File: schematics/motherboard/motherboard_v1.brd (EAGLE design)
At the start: 50 x 50 mm, 66 parts, among them IC1 3.3V, SW1 A6H2101, Y1 25MHz

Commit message: MB PCB update
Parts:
- removed JP5: JTAG_CONNPTH, connectors:AVR_ICSP
- removed JP8: (no value), SparkFun-Retired:SJ_2S-NO
- removed U$2: (no value), Skippy-ExtBoards:BTM400_6B
- added JP26, JP27: (no value), SparkFun-Connectors:1X05
- C15, C3, C4, C5, C6, C9: device SparkFun-Capacitors:1206 -> SparkFun-Capacitors:0805
- JP11: value NEO-6M -> (none); device Skippy-ExtBoards:G6-GPS6MV2 -> SparkFun-Connectors:1X05
- moved JP18 137.7 mm to (44.2, 18.5), turned to 180 degrees
- moved JP17 124.6 mm to (44.2, 28.4), turned to 180 degrees
- moved JP4 120.5 mm to (34.0, 6.35)
- moved JP1 120.3 mm to (46.5, 6.35)
- moved JP3 120.3 mm to (40.1, 6.35)
- moved JP16 117.8 mm to (44.2, 21.8), turned to 180 degrees
- moved C13 116.9 mm to (16.5, 18.5), flipped to the bottom, turned to 135 degrees
- moved D2 116.1 mm to (45.2, 41.4), turned to 90 degrees
- moved C12 115.7 mm to (18.5, 16.5), flipped to the bottom, turned to 135 degrees
- moved C15 115.5 mm to (15.5, 27.4), flipped to the bottom, turned to 45 degrees
- moved JP24 113.2 mm to (48.3, 43.4), turned to 270 degrees
- moved R13 112.5 mm to (5.08, 18.0), flipped to the bottom, turned to 90 degrees
- moved R12 112.5 mm to (5.08, 12.4), flipped to the bottom, turned to 270 degrees
- moved JP15 107.2 mm to (44.2, 25.1), turned to 180 degrees
- moved C10 106.0 mm to (22.1, 23.9), flipped to the bottom, turned to 315 degrees
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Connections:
- removed net JTDO3_TDI2: JP5.9
- removed net JTDO3_TDI4: JP4.3, JP8.1
- new net US_ECHO: JP11.3, U$1.36
- new net US_TRIGGER: JP11.4, U$1.35
- net 3.3V: now also JP26.4, JP27.4; no longer JP11.4, JP5.4, U$2.3.3V
- net DBG_CMD: now also JP26.1; no longer U$2.PIO(11)
- net GND: now also JP26.5, JP27.5; no longer JP5.10, JP5.2, U$2.GND@1, U$2.GND@2, U$2.GND@3, U$2.GND@4
- net JTCK: no longer JP5.1
- net JTDOM: now also JP4.3; no longer JP5.3, JP8.2
- net JTMS: no longer JP5.5
- net RX1: now also JP27.2; no longer JP11.2
- net RX2: now also JP26.2; no longer U$2.UART-TX
- net TX1: now also JP27.3; no longer JP11.3
- net TX2: now also JP26.3; no longer U$2.UART-RX
- net VDD: now also JP11.5
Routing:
- net 3.3V: track 0.00 -> 39.8 mm, vias 0 -> 1
- net GND: track 0.00 -> 21.2 mm, vias 0 -> 3
- net N$3: track 0.00 -> 17.2 mm, vias 0 -> 1
- net N$5: track 0.00 -> 16.4 mm, vias 0 -> 1
- added copper zone on layer 16, net GND

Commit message: Motherboard update with almost-ready routing
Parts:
- added H1, H2, H3, H4: MOUNT-PAD-ROUND3.0, holes:3,0-PAD
- added U$2: SKIPPYTXT-PLC-10MM, skippy-logo:SKIPPYTXT-PLC-10MM
- moved R11 107.4 mm to (45.2, 38.7), turned to 270 degrees
- moved R10 102.6 mm to (45.2, 38.7), flipped to the bottom, turned to 270 degrees
- moved JP25 97.8 mm to (45.3, 33.9), flipped to the bottom, turned to 90 degrees
- moved JP6 57.8 mm to (17.1, 35.8), flipped to the bottom, turned to 180 degrees
- moved JP7 55.0 mm to (17.0, 42.3), flipped to the bottom, turned to 180 degrees
- moved JP27 54.4 mm to (42.4, 40.6), turned to 270 degrees
- moved JP14 47.0 mm to (48.0, 14.4), turned to 270 degrees
- moved JP1 47.0 mm to (8.13, 33.5), turned to 270 degrees
- moved JP12 46.7 mm to (1.78, 26.5)
- moved JP3 45.9 mm to (8.13, 39.2), turned to 270 degrees
- moved JP4 44.9 mm to (14.4, 46.7), turned to 270 degrees
- moved R1 42.8 mm to (6.22, 26.7), turned to 270 degrees
- moved R3 40.2 mm to (28.1, 8.13), turned to 270 degrees
- moved SW1 39.9 mm to (29.3, 8.00)
- moved S1 38.5 mm to (20.8, 8.13), turned to 90 degrees
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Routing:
- net 3.3V: track 39.8 -> 154.6 mm, vias 1 -> 10
- net GND: track 21.2 -> 99.5 mm, vias 3 -> 10
- net SCL1: track 0.00 -> 60.8 mm, vias 0 -> 2
- net VDD: track 0.00 -> 53.8 mm, vias 0 -> 1
- net RX2: track 0.00 -> 52.6 mm, vias 0 -> 1
- net SDA1: track 0.00 -> 51.6 mm, vias 0 -> 2
- net RX3: track 0.00 -> 50.7 mm, vias 0 -> 1
- net JTMS: track 0.00 -> 49.3 mm, vias 0 -> 1
- net DBG_CMD: track 0.00 -> 44.2 mm, vias 0 -> 2
- net N$6: track 0.00 -> 42.0 mm, vias 0 -> 3
- net TX3: track 0.00 -> 40.1 mm, vias 0 -> 2
- net NRST: track 0.00 -> 40.1 mm, vias 0 -> 3
- net PWM7: track 0.00 -> 39.2 mm, vias 0 -> 1
- net TX2: track 0.00 -> 35.0 mm, vias 0 -> 2
- net PWM1: track 0.00 -> 30.5 mm
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- added copper zone on layer 1, net 3.3V

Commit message: Motherboard v1 RTM
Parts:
- added JP5: JUMPER-3SMD, SparkFun-Retired:SJ_3
- moved U$2 31.0 mm to (6.86, 22.2)
- moved R10 20.1 mm to (43.4, 18.7), turned to 90 degrees
- moved JP14 5.08 mm to (48.0, 9.27), turned to 90 degrees
- moved JP10 5.08 mm to (27.3, 48.0), turned to 180 degrees
- moved R14 2.64 mm to (27.4, 39.6), turned to 180 degrees
- moved C8 2.17 mm to (39.5, 43.3)
- moved JP7 2.16 mm to (17.0, 40.1)
- moved JP6 1.53 mm to (17.0, 34.3)
- moved S1 1.53 mm to (20.7, 9.65)
- moved Y1 0.38 mm to (9.65, 14.5)
- moved R11 0.13 mm to (45.3, 38.7), flipped to the bottom
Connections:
- new net N$14: JP10.2
- new net N$16: JP12.2
- new net N$17: JP14.2
- new net N$18: JP13.2
- new net VCCIO: JP15.2, JP16.2, JP17.2, JP18.2, JP5.2
- net 3.3V: now also JP5.3; no longer JP10.2, JP12.2, JP13.2, JP14.2, JP15.2, JP16.2, JP17.2, JP18.2
- net PWM5: now also JP17.3, U$1.39; no longer JP15.3, U$1.37
- net PWM6: now also JP15.3, U$1.37; no longer JP16.3, U$1.38
- net PWM7: now also JP16.3, U$1.38; no longer JP17.3, U$1.39
- net VDD: now also JP5.1
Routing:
- net N$12: track 6.16 -> 22.9 mm
- net RX3: track 50.7 -> 34.5 mm
- net PWM5: track 24.2 -> 39.2 mm, vias 0 -> 1
- net GND: track 99.5 -> 85.8 mm, vias 10 -> 11
- net VCCIO: track 0.00 -> 13.6 mm
- net PWM7: track 39.2 -> 27.8 mm
- net PWM6: track 27.8 -> 24.2 mm, vias 1 -> 0
- net SCL2: track 22.0 -> 25.5 mm
- net 3.3V: track 154.6 -> 151.5 mm
- net JTDO1_TDI2: track 28.7 -> 26.5 mm
- net VDD: track 53.8 -> 55.4 mm
- net JTDOM: track 21.2 -> 22.6 mm
- net N$4: track 5.97 -> 4.97 mm
- net NRST: track 40.1 -> 41.0 mm
- net PWM4: track 26.3 -> 27.1 mm
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- added copper zone on layer 1, net VDD
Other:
- board text added: "+"
- board text added: "-"
- board text added: "3V"
- board text added: "5V"
- board text added: "B0"
- board text added: "B1"
- board text added: "CD"
- board text added: "DTR"
- board text added: "Debug"
- board text added: "EC"
- board text added: "GND"
- board text added: "GPS"
- board text added: "IMU"
- board text added: "I²C1"
- board text added: "I²C2"
- board text added: "JTAG 0"
- board text added: "JTAG 1"
- board text added: "JTAG 2"
- board text added: "LED1"
- board text added: "LED2"
- board text added: "PWM1"
- board text added: "PWM2"
- board text added: "PWM3"
- board text added: "PWM4"
- board text added: "PWM5"
- board text added: "PWM6"
- board text added: "PWM7"
- board text added: "PWM8"
- board text added: "PWR"
- board text added: "RX"
- board text added: "SCL"
- board text added: "SDA"
- board text added: "SRF-04"
- board text added: "TG"
- board text added: "TX"
- board text added: "Telemetry"
- board text added: "~"

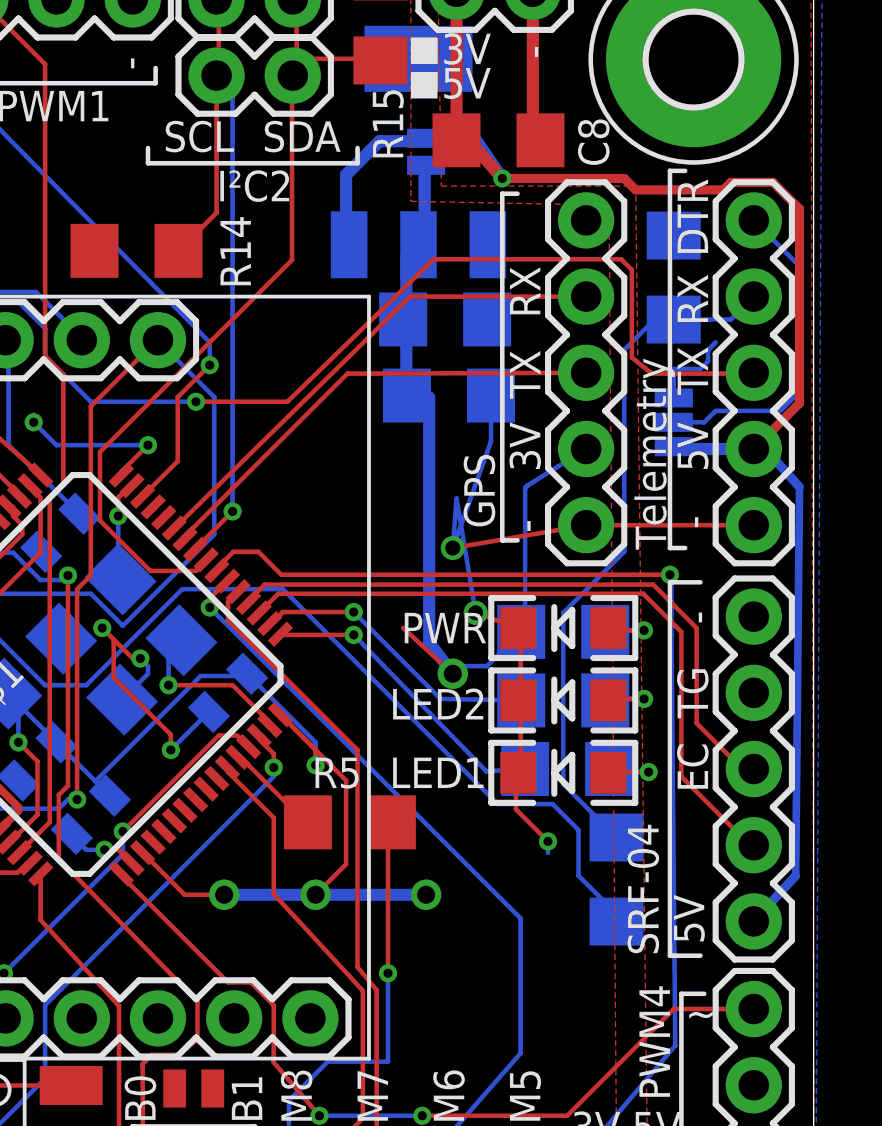
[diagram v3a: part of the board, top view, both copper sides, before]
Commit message: Fixes issues #1 and #2
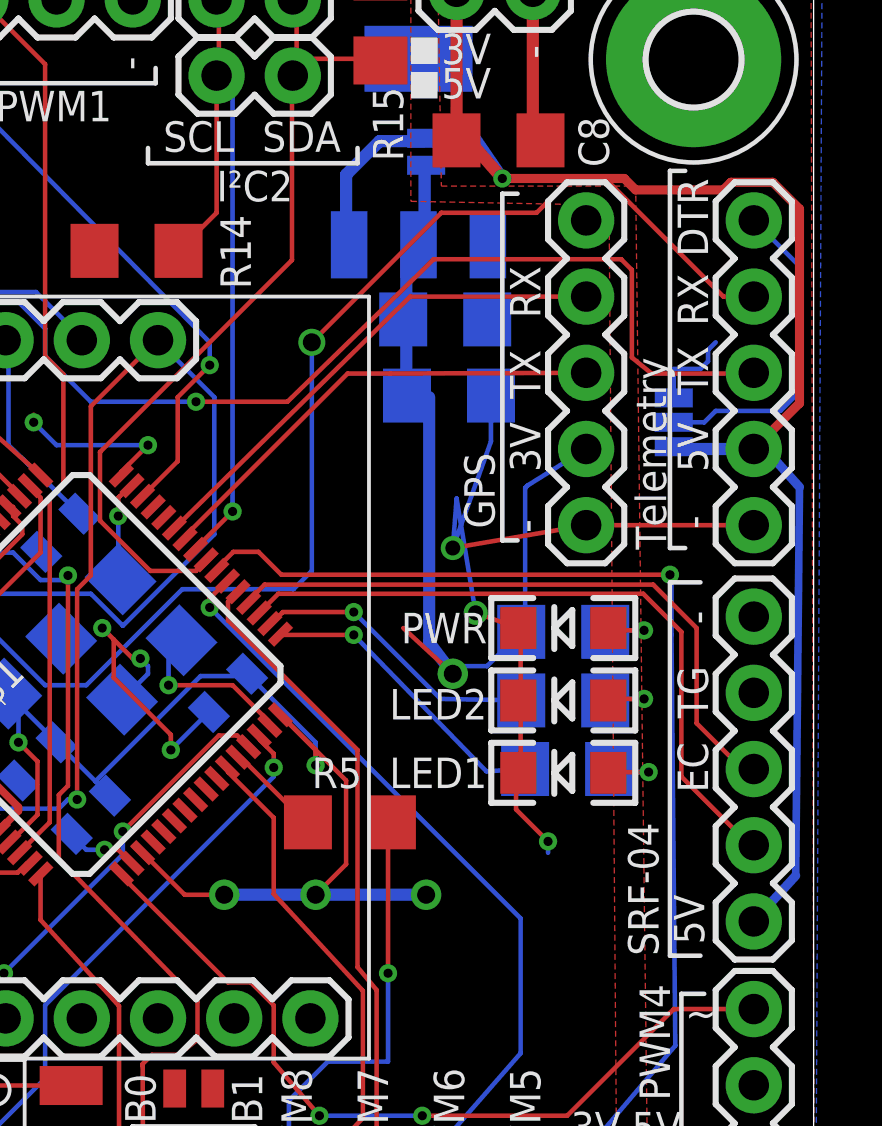
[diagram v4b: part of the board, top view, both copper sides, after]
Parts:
- removed R10: 1K8, SparkFun-Resistors:1206
- removed R11: 3K3, SparkFun-Resistors:1206
- R12, R13: value 4K7 -> 1K5
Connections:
- removed net N$12: JP24.2, R10.2, R11.2
- net GND: no longer R11.1
- net RX3: now also JP24.2; no longer R10.1
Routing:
- net N$12: track 22.9 -> 0.00 mm
- net RX3: track 34.5 -> 45.1 mm, vias 1 -> 2
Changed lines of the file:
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@@
 <?xml version="1.0" encoding="utf-8"?>
 <!DOCTYPE eagle SYSTEM "eagle.dtd">
-<eagle version="6.5.0">
+<eagle version="7.2.0">
 <drawing>
 <settings>
@@
 <pass name="Default">
 <param name="RoutingGrid" value="6mil"/>
+<param name="AutoGrid" value="1"/>
+<param name="Efforts" value="0"/>
+<param name="TopRouterVariant" value="1"/>
 <param name="tpViaShape" value="round"/>
 <param name="PrefDir.1" value="*"/>
@@
 <attribute name="VALUE" x="7.747" y="28.067" size="0.4064" layer="28" rot="MR270"/>
 </element>
-<element name="R10" library="SparkFun-Resistors" package="1206" value="1K8" x="43.434" y="18.669" smashed="yes" rot="MR90">
-<attribute name="NAME" x="44.577" y="17.399" size="1.016" layer="26" rot="MR90"/>
-<attribute name="VALUE" x="41.91" y="17.272" size="0.4064" layer="28" rot="MR90"/>
-</element>
-<element name="R11" library="SparkFun-Resistors" package="1206" value="3K3" x="45.339" y="38.735" smashed="yes" rot="MR270">
-<attribute name="NAME" x="46.482" y="41.275" size="1.016" layer="26" rot="MR0"/>
-<attribute name="VALUE" x="46.863" y="40.132" size="0.4064" layer="28" rot="MR270"/>
-</element>
-<element name="R12" library="SparkFun-Resistors" package="1206" value="4K7" x="5.08" y="12.446" smashed="yes" rot="MR270">
+<element name="R12" library="SparkFun-Resistors" package="1206" value="1K5" x="5.08" y="12.446" smashed="yes" rot="MR270">
 <attribute name="NAME" x="6.477" y="11.303" size="1.016" layer="26" rot="MR90"/>
 <attribute name="VALUE" x="6.604" y="13.843" size="0.4064" layer="28" rot="MR270"/>
 </element>
-<element name="R13" library="SparkFun-Resistors" package="1206" value="4K7" x="5.08" y="18.034" smashed="yes" rot="MR90">
+<element name="R13" library="SparkFun-Resistors" package="1206" value="1K5" x="5.08" y="18.034" smashed="yes" rot="MR90">
 <attribute name="NAME" x="7.366" y="19.304" size="1.016" layer="26" rot="MR270"/>
 <attribute name="VALUE" x="3.556" y="16.637" size="0.4064" layer="28" rot="MR90"/>
@@
 <contactref element="C16" pad="2"/>
 <contactref element="JP24" pad="5"/>
-<contactref element="R11" pad="1"/>
 <contactref element="JP25" pad="3"/>
 <contactref element="JP4" pad="2"/>
@@
 <signal name="RX3">
 <contactref element="U$1" pad="52"/>
-<contactref element="R10" pad="1"/>
 <wire x1="23.3172" y1="30.7848" x2="23.3172" y2="31.0896" width="0.1524" layer="1"/>
 <wire x1="23.622" y1="30.48" x2="23.3172" y2="30.7848" width="0.1524" layer="1"/>
@@
 <wire x1="25.7556" y1="25.146" x2="24.384" y2="25.146" width="0.1524" layer="16"/>
 <wire x1="28.956" y1="28.3464" x2="25.7556" y2="25.146" width="0.1524" layer="16"/>
-<wire x1="32.3088" y1="28.3464" x2="28.956" y2="28.3464" width="0.1524" layer="16"/>
-<wire x1="39.4716" y1="21.1836" x2="32.3088" y2="28.3464" width="0.1524" layer="16"/>
-<wire x1="41.3004" y1="21.1836" x2="39.4716" y2="21.1836" width="0.1524" layer="16"/>
+<wire x1="32.6644" y1="28.3464" x2="28.956" y2="28.3464" width="0.1524" layer="16"/>
 <wire x1="23.3172" y1="31.0896" x2="23.177834375" y2="31.090140625" width="0.1524" layer="1"/>
 <via x="22.4028" y="28.956" extent="1-16" drill="0.3048"/>
-<wire x1="43.434" y1="17.269" x2="43.434" y2="17.526" width="0.1524" layer="16"/>
-<wire x1="43.434" y1="17.526" x2="42.164" y2="18.796" width="0.1524" layer="16"/>
-<wire x1="42.164" y1="18.796" x2="42.164" y2="20.32" width="0.1524" layer="16"/>
-<wire x1="42.164" y1="20.32" x2="41.3004" y2="21.1836" width="0.1524" layer="16"/>
+<contactref element="JP24" pad="2"/>
+<wire x1="32.6644" y1="28.3464" x2="33.274" y2="28.956" width="0.1524" layer="16"/>
+<wire x1="33.274" y1="28.956" x2="33.274" y2="36.576" width="0.1524" layer="16"/>
+<via x="33.274" y="36.576" extent="1-16" drill="0.6" shape="square"/>
+<wire x1="33.274" y1="36.576" x2="37.592" y2="40.894" width="0.1524" layer="1"/>
+<wire x1="37.592" y1="40.894" x2="40.767" y2="40.894" width="0.1524" layer="1"/>
+<wire x1="40.767" y1="40.894" x2="41.783" y2="41.91" width="0.1524" layer="1"/>
+<wire x1="41.783" y1="41.91" x2="43.18" y2="41.91" width="0.1524" layer="1"/>
+<wire x1="43.18" y1="41.91" x2="46.99" y2="38.1" width="0.1524" layer="1"/>
+<wire x1="46.99" y1="38.1" x2="48.006" y2="38.1" width="0.1524" layer="1"/>
 </signal>
 <signal name="DBG_CMD">
@@
 </polygon>
 </signal>
-<signal name="N$12">
-<contactref element="R10" pad="2"/>
-<contactref element="JP24" pad="2"/>
-<contactref element="R11" pad="2"/>
-<wire x1="48.009" y1="38.097" x2="48.006" y2="38.1" width="0.1524" layer="1"/>
-<wire x1="45.339" y1="37.335" x2="47.241" y2="37.335" width="0.1524" layer="16"/>
-<wire x1="47.241" y1="37.335" x2="48.006" y2="38.1" width="0.1524" layer="16"/>
-<wire x1="45.339" y1="37.335" x2="44.701" y2="37.335" width="0.1524" layer="16"/>
-<wire x1="44.701" y1="37.335" x2="43.688" y2="36.322" width="0.1524" layer="16"/>
-<wire x1="43.688" y1="36.322" x2="43.688" y2="29.591" width="0.1524" layer="16"/>
-<wire x1="43.688" y1="29.591" x2="41.656" y2="27.559" width="0.1524" layer="16"/>
-<wire x1="41.656" y1="27.559" x2="41.656" y2="21.847" width="0.1524" layer="16"/>
-<wire x1="41.656" y1="21.847" x2="43.434" y2="20.069" width="0.1524" layer="16"/>
-</signal>
 <signal name="N$13">
